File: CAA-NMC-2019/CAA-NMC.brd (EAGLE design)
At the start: 33.3 x 100 mm, 28 parts, among them IC1 ATTINY85-20SU, J1 M20-9980346

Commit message: Isolated battery/USB power supplies at switch
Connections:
- net GND: now also U$1.GND10, U$1.GND11, U$1.GND12, U$2.GND, U$3.GND
- net VBAT: now also U$2.VBAT, U$3.VBAT
- net VCC: now also U$1.PWR10, U$1.PWR11, U$1.PWR12; no longer J1.VCC
- net VUSB: now also J1.VCC
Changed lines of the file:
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@@
 <signal name="VCC" class="1">
 <contactref element="IC1" pad="VCC"/>
-<contactref element="J1" pad="VCC"/>
 <contactref element="U$74" pad="P$1"/>
 <contactref element="U$123" pad="P$2"/>
@@
 <contactref element="R2" pad="2"/>
 <contactref element="U$145" pad="5"/>
+<contactref element="U$1" pad="PWR10"/>
+<contactref element="U$1" pad="PWR11"/>
+<contactref element="U$1" pad="PWR12"/>
 <wire x1="11.436" y1="90.64" x2="13.916" y2="97.5869" width="0" layer="19" extent="1-1"/>
 <wire x1="9.48895" y1="85.302378125" x2="11.436" y2="90.64" width="0" layer="19" extent="1-1"/>
@@
 <wire x1="-7.838" y1="62.973" x2="0.895" y2="68.573" width="0" layer="19" extent="1-1"/>
 <wire x1="-9.515" y1="68.573" x2="-7.838" y2="62.973" width="0" layer="19" extent="1-1"/>
-<wire x1="-13.97" y1="49.942" x2="-7.838" y2="62.973" width="0" layer="19" extent="1-1"/>
+<wire x1="-13.97" y1="57.562" x2="-7.838" y2="62.973" width="0" layer="19" extent="1-1"/>
+<wire x1="-13.97" y1="55.022" x2="-13.97" y2="57.562" width="0" layer="19" extent="1-1"/>
+<wire x1="-13.97" y1="52.482" x2="-13.97" y2="55.022" width="0" layer="19" extent="1-1"/>
+<wire x1="-13.97" y1="49.942" x2="-13.97" y2="52.482" width="0" layer="19" extent="1-1"/>
 <wire x1="-13.97" y1="47.402" x2="-13.97" y2="49.942" width="0" layer="19" extent="1-1"/>
 <wire x1="-13.97" y1="44.862" x2="-13.97" y2="47.402" width="0" layer="19" extent="1-1"/>
@@
 <wire x1="-13.97" y1="29.622" x2="-13.97" y2="32.162" width="0" layer="19" extent="1-1"/>
 <wire x1="-13.97" y1="27.082" x2="-13.97" y2="29.622" width="0" layer="19" extent="1-1"/>
-<wire x1="-8.542059375" y1="94.195115625" x2="9.48895" y2="85.302378125" width="0" layer="19" extent="1-1"/>
-<wire x1="-25.576" y1="85.227" x2="-8.542059375" y2="94.195115625" width="0" layer="19" extent="1-1"/>
+<wire x1="-25.576" y1="85.227" x2="-9.515" y2="68.573" width="0" layer="19" extent="1-1"/>
 <wire x1="45.48" y1="17.905" x2="12.997" y2="62.973" width="0" layer="19" extent="1-1"/>
 </signal>
@@
 <contactref element="D3" pad="GND"/>
 <contactref element="D3" pad="CAP1"/>
+<contactref element="U$2" pad="GND"/>
+<contactref element="U$3" pad="GND"/>
 <wire x1="8.896" y1="90.64" x2="6.416" y2="93.7769" width="0" layer="19" extent="1-1"/>
 <wire x1="-13.622059375" y1="94.195115625" x2="6.416" y2="93.7769" width="0" layer="19" extent="1-1"/>
@@
 <wire x1="13.97" y1="29.622" x2="13.97" y2="32.162" width="0" layer="19" extent="1-1"/>
 <wire x1="13.97" y1="27.082" x2="13.97" y2="29.622" width="0" layer="19" extent="1-1"/>
-<wire x1="37.86" y1="17.905" x2="13.97" y2="27.082" width="0" layer="19" extent="1-1"/>
+<wire x1="14.65" y1="12.504" x2="13.97" y2="27.082" width="0" layer="19" extent="1-1"/>
+<wire x1="8.15" y1="12.504" x2="14.65" y2="12.504" width="0" layer="19" extent="1-1"/>
+<wire x1="37.86" y1="17.905" x2="14.65" y2="12.504" width="0" layer="19" extent="1-1"/>
 <wire x1="-33.577" y1="47.6" x2="-12.992" y2="66.173" width="0" layer="19" extent="1-1"/>
 <wire x1="-40.577" y1="47.6" x2="-33.577" y2="47.6" width="0" layer="19" extent="1-1"/>
@@
 <wire x1="-40.577" y1="39.6" x2="-40.577" y2="47.6" width="0" layer="19" extent="1-1"/>
 <wire x1="-38.15" y1="32" x2="-40.577" y2="39.6" width="0" layer="19" extent="1-1"/>
+<contactref element="U$1" pad="GND10"/>
+<contactref element="U$1" pad="GND11"/>
+<contactref element="U$1" pad="GND12"/>
 </signal>
 <signal name="PB2">
@@
 <signal name="VBAT">
 <contactref element="U$145" pad="4"/>
+<contactref element="U$3" pad="VBAT"/>
+<contactref element="U$2" pad="VBAT"/>
+<wire x1="-11.85" y1="12.504" x2="6.98895" y2="85.302378125" width="0" layer="19" extent="1-1"/>
+<wire x1="-14.65" y1="12.504" x2="-11.85" y2="12.504" width="0" layer="19" extent="1-1"/>
 </signal>
 <signal name="VUSB">
 <contactref element="U$145" pad="6"/>
+<contactref element="J1" pad="VCC"/>
+<wire x1="-8.542059375" y1="94.195115625" x2="11.98895" y2="85.302378125" width="0" layer="19" extent="1-1"/>
 </signal>
 </signals>

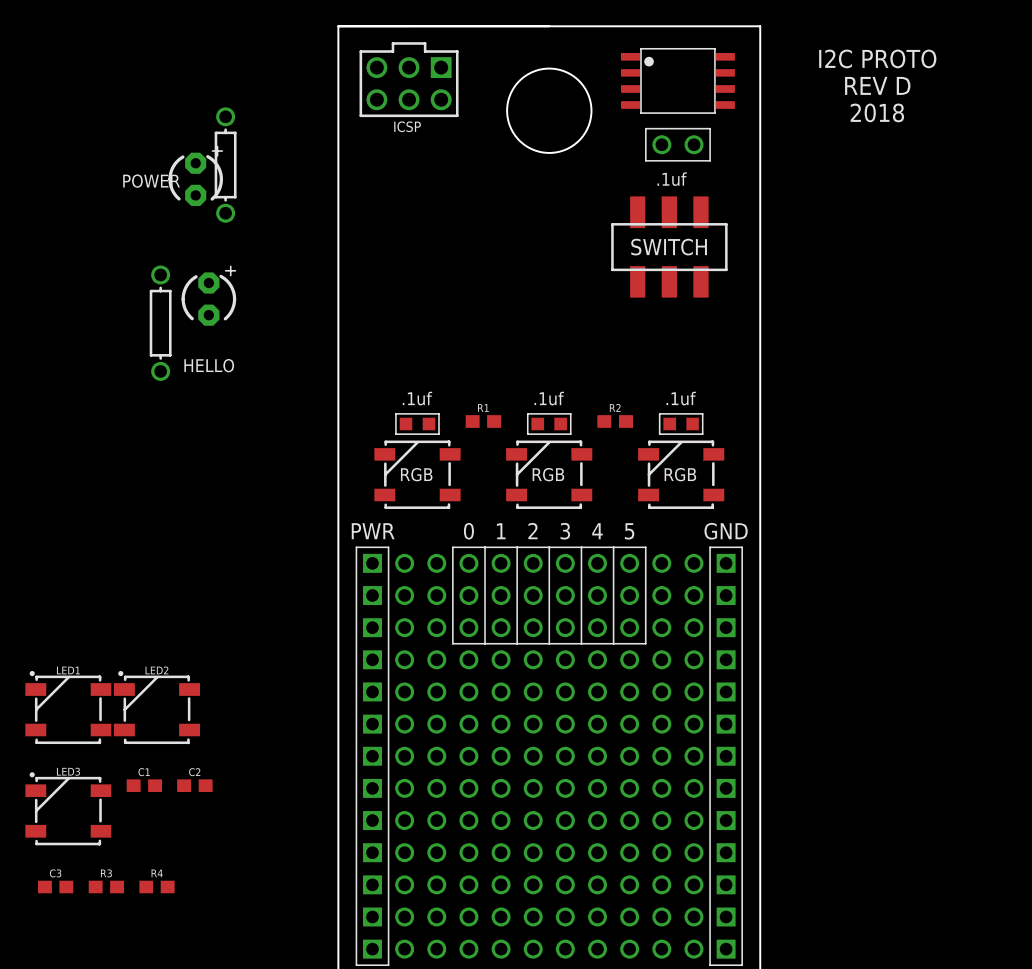
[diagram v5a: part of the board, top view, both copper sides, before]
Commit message: restored most parts to layout
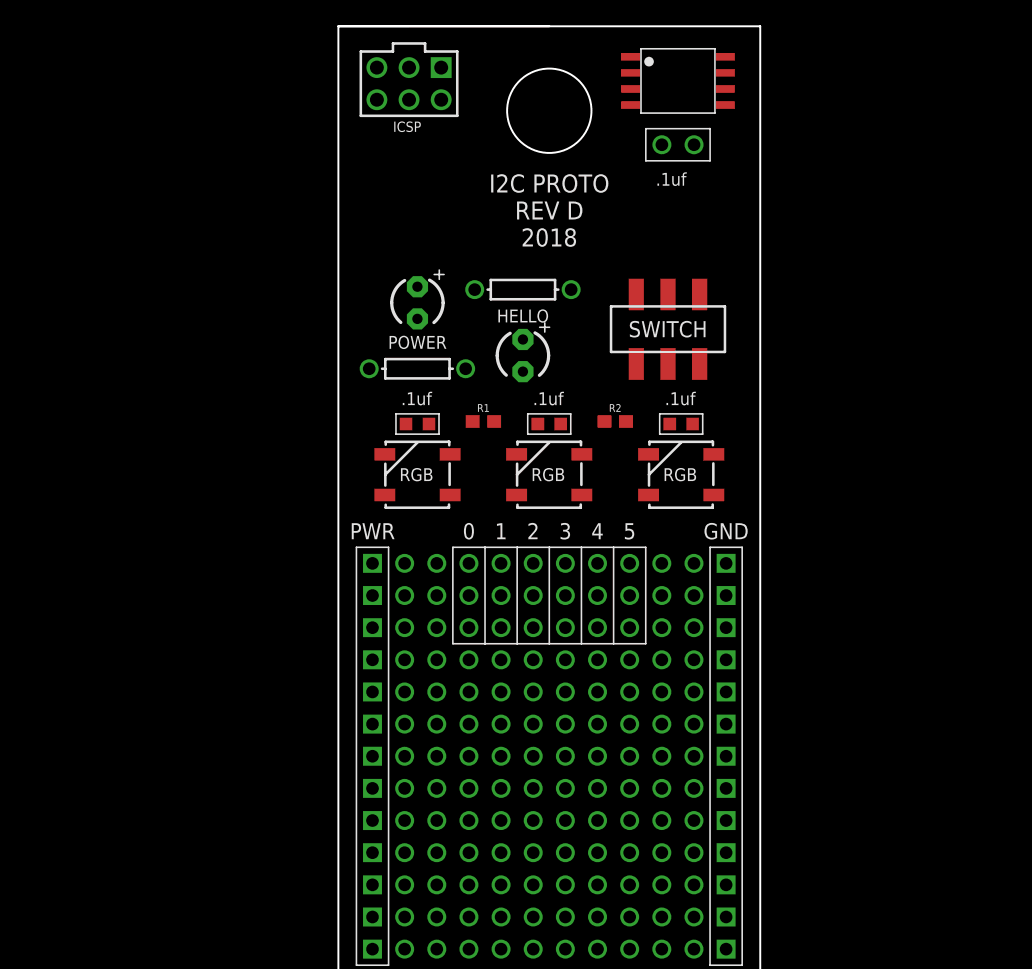
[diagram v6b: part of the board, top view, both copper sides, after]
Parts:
- removed C1, C2, C3: 0.1uF, SparkFun-Capacitors:0603
- removed LED1, LED2, LED3: WS2812B, SparkFun-LED:WS2812B
- removed R3: 470, SparkFun-Resistors:0603
- removed R4: 10k, SparkFun-Resistors:0603
- moved POWER 29.4 mm to (-2.08, 74.0)
- moved U$127 28.7 mm to (-2.08, 79.2), turned to 0 degrees
- moved U$126 22.1 mm to (-10.4, 72.9), turned to 0 degrees
- moved HELLO 16.5 mm to (-10.4, 78.2)
- moved U$145 6.49 mm to (9.38, 76.1)
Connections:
- removed net N$10: LED2.2, LED3.4
- removed net N$12: LED1.4, R3.1
- removed net N$9: LED1.2, LED2.4
- removed net RGBLEDS: R3.2, R4.1
- removed net VDD: C1.1, C2.1, C3.1, LED1.1, LED2.1, LED3.1, R4.2
- net GND: no longer C1.2, C2.2, C3.2, LED1.3, LED2.3, LED3.3

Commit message: all together now
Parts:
- removed U$71: GND, BadgeParts:1X01
- removed U$72: SDA, BadgeParts:1X01
- removed U$73: SCL, BadgeParts:1X01
- removed U$74: VCC, BadgeParts:1X01
- added U$4: I2C-PADS, BadgeParts:I2C-PADS
- moved J1 21.9 mm to (10.8, 92.9)
- moved IC1 21.5 mm to (-9.63, 87.3)
- moved U$123 13.1 mm to (-2.57, 84.4), turned to 90 degrees
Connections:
- net GND: now also U$4.GND; no longer U$71.P$1
- net PB0: now also U$4.SDA; no longer U$72.P$1
- net PB2: now also U$4.SCL; no longer U$73.P$1
- net VCC: now also U$4.VCC; no longer U$74.P$1
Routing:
- net GND: track 0.00 -> 181.9 mm, vias 0 -> 2
- net VCC: track 0.00 -> 136.9 mm, vias 0 -> 2
- net PB5: track 0.00 -> 82.1 mm
- net VBAT: track 0.00 -> 76.9 mm, vias 0 -> 1
- net PB2: track 0.00 -> 75.2 mm, vias 0 -> 1
- net PB0: track 0.00 -> 73.7 mm
- net PB4: track 0.00 -> 71.0 mm
- net PB1: track 0.00 -> 62.4 mm, vias 0 -> 1
- net PB3: track 0.00 -> 43.0 mm
- net VUSB: track 0.00 -> 16.0 mm
- net N$1: track 0.00 -> 13.1 mm
- net N$5: track 0.00 -> 9.34 mm
- net N$4: track 0.00 -> 6.59 mm
- net N$3: track 0.00 -> 6.57 mm
- net N$2: track 0.00 -> 4.64 mm
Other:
- board text added: "ATTINY PROTO RUN NMC 2018"
- board text removed: "GND"
- board text removed: "I2C PROTO REV D 2018"
- board text removed: "SCL"
- board text removed: "SDA"
- board text removed: "VCC"

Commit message: aligning parts
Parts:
- moved U$123 7.14 mm to (-8.36, 88.6), turned to 180 degrees
- moved IC1 3.13 mm to (-9.63, 84.2)
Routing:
- net GND: track 181.9 -> 0.00 mm, vias 2 -> 0
- net VCC: track 136.9 -> 0.00 mm, vias 2 -> 0
- net PB5: track 82.1 -> 0.00 mm
- net VBAT: track 76.9 -> 0.00 mm, vias 1 -> 0
- net PB2: track 75.2 -> 0.00 mm, vias 1 -> 0
- net PB0: track 73.7 -> 0.00 mm
- net PB4: track 71.0 -> 0.00 mm
- net PB1: track 62.4 -> 0.00 mm, vias 1 -> 0
- net PB3: track 43.0 -> 0.00 mm
- net VUSB: track 16.0 -> 0.00 mm
- net N$1: track 13.1 -> 0.00 mm
- net N$5: track 9.34 -> 0.00 mm
- net N$4: track 6.59 -> 0.00 mm
- net N$3: track 6.57 -> 0.00 mm
- net N$2: track 4.64 -> 0.00 mm
